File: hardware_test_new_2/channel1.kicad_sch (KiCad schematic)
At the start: 20 parts, among them J3 XT60_MALE, Q4 BSC070N10NS5, U5 INA180A1

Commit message: test2 schematic
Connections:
- net CHA_SHUNT+ is gone; now on net CH_SHUNT+: R5.2
- net CHA_SHUNT- is gone; now on net CH_SHUNT-: R5.3

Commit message: test2 schematic should ok
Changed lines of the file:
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@@
+	(wire
+		(pts
+			(xy 49.53 72.39) (xy 52.07 72.39)
+		)
+		(stroke
+			(width 0)
+			(type default)
+		)
+	)
 	(wire
 		(pts
@@
 	(wire
 		(pts
-			(xy 106.68 52.07) (xy 106.68 46.99)
-		)
-		(stroke
-			(width 0)
-			(type default)
-		)
-	)
-	(wire
-		(pts
 			(xy 54.61 52.07) (xy 52.07 52.07)
 		)
@@
 	(wire
 		(pts
-			(xy 110.49 52.07) (xy 113.03 52.07)
+			(xy 102.87 52.07) (xy 113.03 52.07)
 		)
 		(stroke
@@
 	(wire
 		(pts
+			(xy 49.53 77.47) (xy 52.07 77.47)
+		)
+		(stroke
+			(width 0)
+			(type default)
+		)
+	)
+	(wire
+		(pts
 			(xy 104.14 74.93) (xy 101.6 74.93)
 		)
@@
 	(wire
 		(pts
-			(xy 106.68 46.99) (xy 113.03 46.99)
+			(xy 102.87 46.99) (xy 113.03 46.99)
 		)
 		(stroke
@@
 			(width 0)
 			(type default)
+		)
+	)
+	(label "CH_SHUNT-"
+		(at 102.87 52.07 0)
+		(effects
+			(font
+				(size 1.27 1.27)
+			)
+			(justify left bottom)
+		)
+	)
+	(label "CH_SHUNT+"
+		(at 49.53 72.39 180)
+		(effects
+			(font
+				(size 1.27 1.27)
+			)
+			(justify right bottom)
+		)
+	)
+	(label "CH_SHUNT+"
+		(at 102.87 46.99 0)
+		(effects
+			(font
+				(size 1.27 1.27)
+			)
+			(justify left bottom)
+		)
+	)
+	(label "CH_SHUNT-"
+		(at 49.53 77.47 180)
+		(effects
+			(font
+				(size 1.27 1.27)
+			)
+			(justify right bottom)
 		)
 	)
@@
 		)
 	)
-	(hierarchical_label "CH_SHUNT-"
-		(shape input)
-		(at 52.07 77.47 180)
-		(effects
-			(font
-				(size 1.27 1.27)
-			)
-			(justify right)
-		)
-	)
 	(hierarchical_label "CH_SW"
 		(shape input)
@@
 		(effects
 			(font
-				(size 1.27 1.27)
-			)
-			(justify right)
-		)
-	)
-	(hierarchical_label "CH_SHUNT+"
-		(shape input)
-		(at 106.68 52.07 270)
-		(effects
-			(font
-				(size 1.27 1.27)
-			)
-			(justify right)
-		)
-	)
-	(hierarchical_label "CH_SHUNT+"
-		(shape input)
-		(at 52.07 72.39 180)
-		(effects
-			(font
-				(size 1.27 1.27)
-			)
-			(justify right)
-		)
-	)
-	(hierarchical_label "CH_SHUNT-"
-		(shape input)
-		(at 110.49 52.07 270)
-		(effects
-			(font

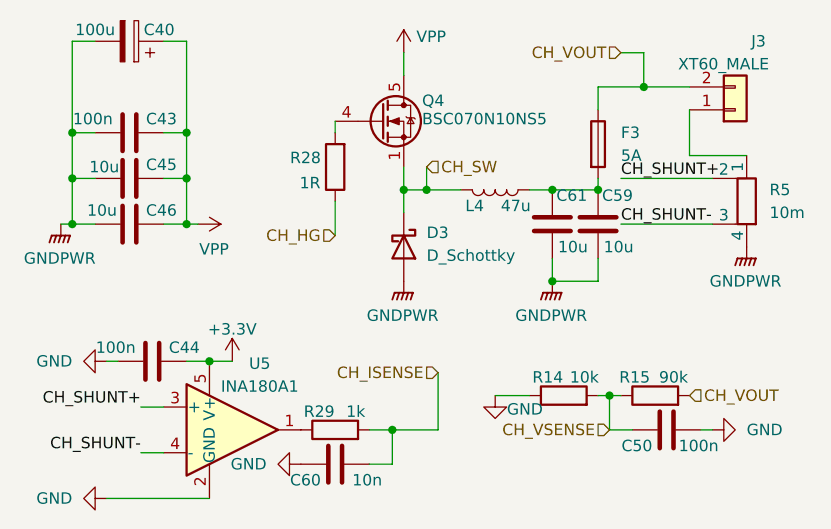
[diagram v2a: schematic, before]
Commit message: new Hardware manufactured
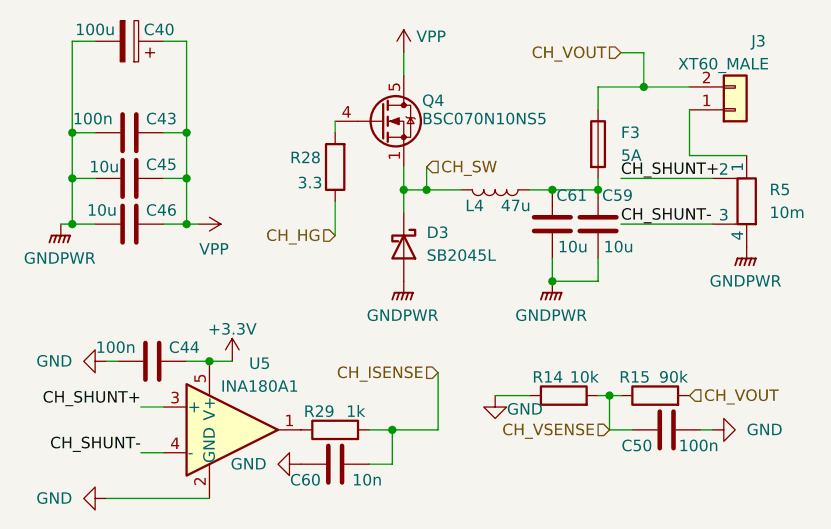
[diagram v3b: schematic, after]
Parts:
- D3: value D_Schottky -> SB2045L
- R28: value 1R -> 3.3
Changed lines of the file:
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@@
 			)
 		)
-		(property "Value" "D_Schottky"
+		(property "Value" "SB2045L"
 			(at 81.28 55.5624 90)
 			(effects
@@
 			)
 		)
-		(property "Value" "1R"
+		(property "Value" "3.3"
 			(at 68.326 47.498 0)
 			(effects
